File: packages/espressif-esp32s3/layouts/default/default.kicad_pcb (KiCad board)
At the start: 2 copper layers, 9 parts

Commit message: Esp32s3
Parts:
- removed R3: 10kΩ ±1% 100mW, UNI_ROYAL_0603WAF1002T5E:R0603
- moved SW1 174.4 mm to (150.9, 102.8), turned to -90 degrees
- moved R2 157.2 mm to (129.0, 89.8), turned to -90 degrees
- moved SW2 142.5 mm to (127.6, 93.4), turned to 90 degrees
- moved R1 35.1 mm to (150.3, 106.3), turned to 180 degrees
- moved C3 23.4 mm to (127.5, 96.7), turned to 180 degrees
- moved C1 17.0 mm to (127.5, 88.4)
- moved C2 16.9 mm to (129.0, 87.8)
- moved U1 16.9 mm to (139.3, 96.1)
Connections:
- R1 pad 2: enable-output -> io[0]-output
- R2 pad 2: io[0]-output -> enable-output
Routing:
- net GND: track 0.00 -> 8.64 mm
- net enable-output: track 0.00 -> 8.62 mm
- net io[0]-output: track 0.00 -> 7.88 mm
- net VCC: track 0.00 -> 6.19 mm, vias 0 -> 1
- net 12: track 4.99 -> 0.00 mm
- net 21: track 4.53 -> 0.00 mm, vias 1 -> 0
- net 8: track 2.88 -> 0.00 mm

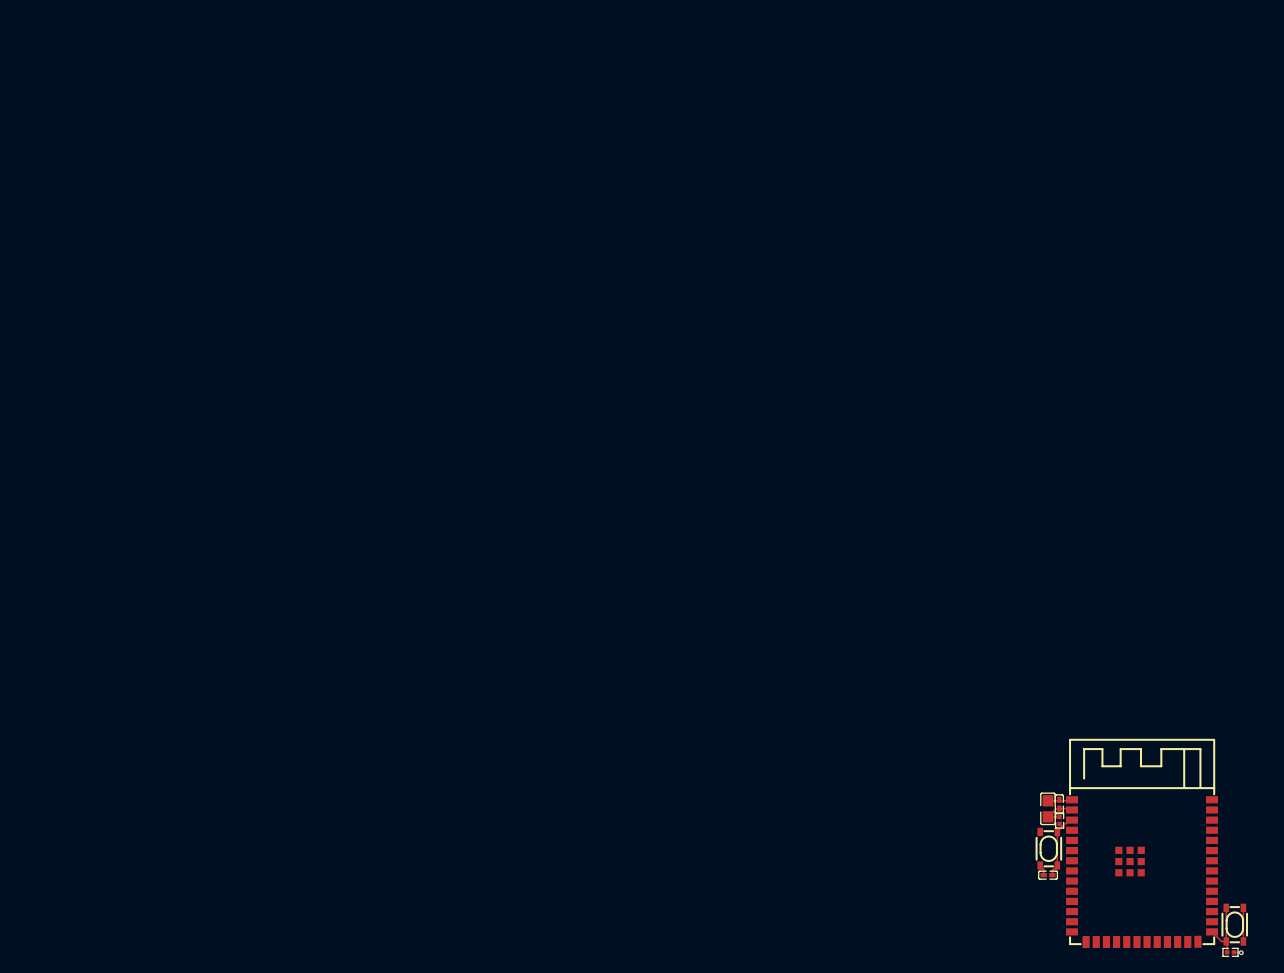
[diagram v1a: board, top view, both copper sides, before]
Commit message: update buttons dep
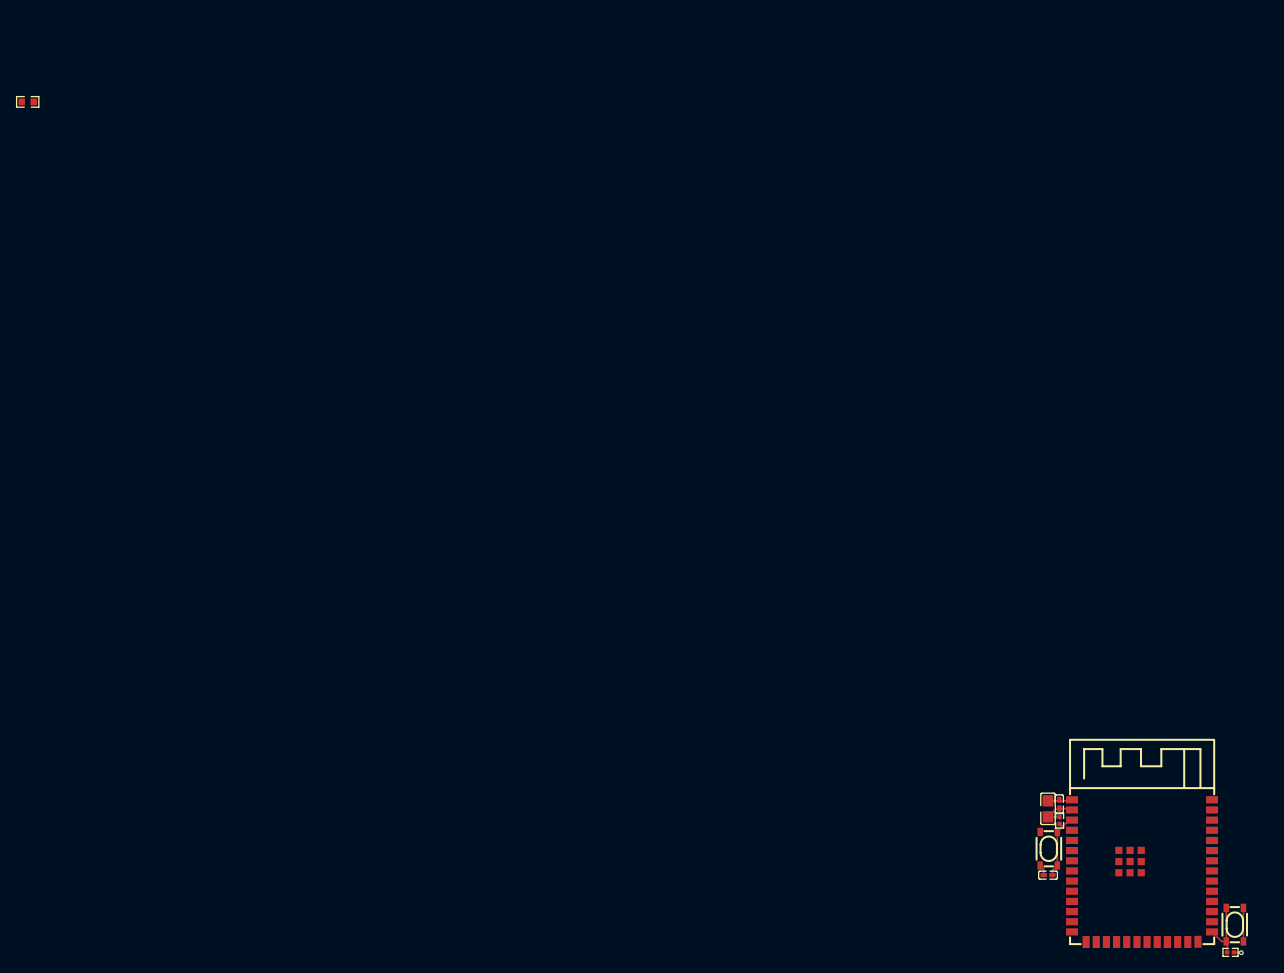
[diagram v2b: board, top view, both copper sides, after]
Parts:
- added R3: 10kΩ ±1% 100mW, UNI_ROYAL_0603WAF1002T5E:R0603, F.Cu at (0.00, 0.00)

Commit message: shipped dev board
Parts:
- removed R3: 10kΩ ±1% 100mW, UNI_ROYAL_0603WAF1002T5E:R0603
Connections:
- net IO15 renamed io[15]-line
- net IO16 renamed io[16]-line
- net IO17 renamed io[17]-line
- net IO18 renamed io[18]-line
